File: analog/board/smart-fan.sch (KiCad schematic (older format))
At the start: 31 parts, among them J1 Conn_01x03_MountingPin, J2 Barrel_Jack, J3 Screw_Terminal_01x02, J4 Conn_01x03_Male, Q1 BC817, Q2 Q_PMOS_GSD, Q3 Q_PMOS_GSD, Q4 BC817, U1 MCP602, U2 AMS1117-5.0, U3 NE555P

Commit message: Working on analog board layout
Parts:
- J1: value Conn_01x03_MountingPin -> TEMP_In; footprint Connector_Pin127mm:PinHeader_1x03_P1.27mm_Vertical -> Connector_PinHeader_1.27mm:PinHeader_1x03_P1.27mm_Vertical; symbol ConnectorMountingPin:Conn_01x03_MountingPin -> smart-fan-rescue:Conn_01x03_MountingPin-ConnectorMountingPin
- J2: value Barrel_Jack -> 12V_PWR
- J3: value Screw_Terminal_01x02 -> 12V_In; footprint Connector_PinSocket254mm:PinSocket_1x02_P2.54mm_Vertical -> Connector_PinSocket_2.54mm:PinSocket_1x02_P2.54mm_Vertical
- J4: value Conn_01x03_Male -> FAN_Out; footprint Connector_Pin127mm:PinHeader_1x03_P1.27mm_Vertical -> Connector_JST:JST_EH_B3B-EH-A_1x03_P2.50mm_Vertical
- Q1, Q4: symbol TransistorBJT:BC817 -> smart-fan-rescue:BC817-TransistorBJT
- RV1: footprint Resistor_SMD:R_0805_2012Metric_Pad1.15x1.40mm_HandSolder -> Potentiometer_THT:Potentiometer_Bourns_3266Y_Vertical
- U1: footprint Package_SO:SOIC-8_3.9x4.9mm_P1.27mm -> Package_SO:SOIC-8_5.275x5.275mm_P1.27mm; symbol AmpOperational:MCP602 -> smart-fan-rescue:MCP602-AmpOperational
- U2: symbol Reg_Linear:AMS1117-5.0 -> smart-fan-rescue:AMS1117-5.0-Reg_Linear
- U3: footprint Package_DIP:DIP-8_W7.62mm -> Package_SO:SOIC-8_5.275x5.275mm_P1.27mm
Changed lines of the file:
@@
 $EndDescr
 $Comp
-L Reg_Linear:AMS1117-5.0 U2
+L smart-fan-rescue:AMS1117-5.0-Reg_Linear U2
 U 1 1 5EE1376A
 P 1400 1200
@@
 	850  1650 850  1500
 $Comp
-L AmpOperational:MCP602 U1
+L smart-fan-rescue:MCP602-AmpOperational U1
 U 1 1 5EE1D336
 P 3400 2450
 F 0 "U1" H 3400 2817 50  0000 C CNN
 F 1 "MCP602" H 3400 2726 50  0000 C CNN
-F 2 "Package_SO:SOIC-8_3.9x4.9mm_P1.27mm" H 3400 2450 50  0001 C CNN
+F 2 "Package_SO:SOIC-8_5.275x5.275mm_P1.27mm" H 3400 2450 50  0001 C CNN
 F 3 "http://ww1.microchip.com/downloads/en/DeviceDoc/21314g.pdf" H 3400 2450 50  0001 C CNN
 	1    3400 2450
@@
 $EndComp
 $Comp
-L AmpOperational:MCP602 U1
+L smart-fan-rescue:MCP602-AmpOperational U1
 U 2 1 5EE20815
 P 5150 2350
 F 0 "U1" H 5150 2717 50  0000 C CNN
 F 1 "MCP602" H 5150 2626 50  0000 C CNN
-F 2 "Package_SO:SOIC-8_3.9x4.9mm_P1.27mm" H 5150 2350 50  0001 C CNN
+F 2 "Package_SO:SOIC-8_5.275x5.275mm_P1.27mm" H 5150 2350 50  0001 C CNN
 F 3 "http://ww1.microchip.com/downloads/en/DeviceDoc/21314g.pdf" H 5150 2350 50  0001 C CNN
 	2    5150 2350
@@
 $EndComp
 $Comp
-L AmpOperational:MCP602 U1
+L smart-fan-rescue:MCP602-AmpOperational U1
 U 3 1 5EE2DBB3
 P 1000 3400
 F 0 "U1" H 958 3446 50  0000 L CNN
 F 1 "MCP602" H 958 3355 50  0000 L CNN
-F 2 "Package_SO:SOIC-8_3.9x4.9mm_P1.27mm" H 1000 3400 50  0001 C CNN
+F 2 "Package_SO:SOIC-8_5.275x5.275mm_P1.27mm" H 1000 3400 50  0001 C CNN
 F 3 "http://ww1.microchip.com/downloads/en/DeviceDoc/21314g.pdf" H 1000 3400 50  0001 C CNN
 	3    1000 3400
@@
 F 0 "RV1" H 4232 1896 50  0000 R CNN
 F 1 "10k" H 4232 1805 50  0000 R CNN
-F 2 "Resistor_SMD:R_0805_2012Metric_Pad1.15x1.40mm_HandSolder" H 4300 1850 50  0001 C CNN
+F 2 "Potentiometer_THT:Potentiometer_Bourns_3266Y_Vertical" H 4300 1850 50  0001 C CNN
 F 3 "~" H 4300 1850 50  0001 C CNN
 	1    4300 1850
@@
 $EndComp
 $Comp
-L TransistorBJT:BC817 Q4
+L smart-fan-rescue:BC817-TransistorBJT Q4
 U 1 1 5EE5A90C
 P 6900 2650
@@
 F 0 "U3" H 3000 5431 50  0000 C CNN
 F 1 "NE555P" H 3000 5340 50  0000 C CNN
-F 2 "Package_DIP:DIP-8_W7.62mm" H 3650 4450 50  0001 C CNN
+F 2 "Package_SO:SOIC-8_5.275x5.275mm_P1.27mm" H 3650 4450 50  0001 C CNN
 F 3 "http://www.ti.com/lit/ds/symlink/ne555.pdf" H 3850 4450 50  0001 C CNN
 	1    3000 4850
@@
 $EndComp
 $Comp
-L TransistorBJT:BC817 Q1
+L smart-fan-rescue:BC817-TransistorBJT Q1
 U 1 1 5EE8608C
 P 4950 4650
@@
 	3500 4650 4350 4650
 $Comp
-L ConnectorMountingPin:Conn_01x03_MountingPin J1
+L smart-fan-rescue:Conn_01x03_MountingPin-ConnectorMountingPin J1
 U 1 1 5EEE3110
 P 2150 2350
 F 0 "J1" H 2238 2222 50  0000 L CNN
-F 1 "Conn_01x03_MountingPin" H 2238 2313 50  0000 L CNN
-F 2 "Connector_Pin127mm:PinHeader_1x03_P1.27mm_Vertical" H 2150 2350 50  0001 C CNN
+F 1 "TEMP_In" H 2238 2313 50  0000 L CNN
+F 2 "Connector_PinHeader_1.27mm:PinHeader_1x03_P1.27mm_Vertical" H 2150 2350 50  0001 C CNN
 F 3 "~" H 2150 2350 50  0001 C CNN
 	1    2150 2350
@@
 P 3100 1000
 F 0 "J2" H 3157 1325 50  0000 C CNN
-F 1 "Barrel_Jack" H 3157 1234 50  0000 C CNN
+F 1 "12V_PWR" H 3157 1234 50  0000 C CNN
 F 2 "Connector_BarrelJack:BarrelJack_CUI_PJ-063AH_Horizontal_CircularHoles" H 3150 960 50  0001 C CNN
 F 3 "~" H 3150 960 50  0001 C CNN
@@
 P 4200 950
 F 0 "J3" H 4280 942 50  0000 L CNN
-F 1 "Screw_Terminal_01x02" H 4280 851 50  0000 L CNN
-F 2 "Connector_PinSocket254mm:PinSocket_1x02_P2.54mm_Vertical" H 4200 950 50  0001 C CNN
+F 1 "12V_In" H 4280 851 50  0000 L CNN
+F 2 "Connector_PinSocket_2.54mm:PinSocket_1x02_P2.54mm_Vertical" H 4200 950 50  0001 C CNN
 F 3 "~" H 4200 950 50  0001 C CNN
 	1    4200 950
@@
 Connection ~ 3550 1100
 $Comp
-L Power:+5V #PWR0101
+L smart-fan-rescue:+5V-Power #PWR0101
 U 1 1 5EF075B6
 P 4300 1450
@@
 $EndComp
 $Comp
-L Power:+5V #PWR0102
+L smart-fan-rescue:+5V-Power #PWR0102
 U 1 1 5EF08EF6
 P 6150 1650
@@
 $EndComp
 $Comp
-L Power:+5V #PWR0103
+L smart-fan-rescue:+5V-Power #PWR0103
 U 1 1 5EF093BB
 P 1900 850
@@
 $EndComp
 $Comp
-L Power:+5V #PWR0104
+L smart-fan-rescue:+5V-Power #PWR0104
 U 1 1 5EF099FD
 P 2500 2100
@@
 $EndComp
 $Comp
-L Power:+5V #PWR0105
+L smart-fan-rescue:+5V-Power #PWR0105
 U 1 1 5EF0D3EB
 P 1150 2750
@@
 	1150 2750 1150 2900
 $Comp
-L Power:GND #PWR0106
+L smart-fan-rescue:GND-Power #PWR0106
 U 1 1 5EF0F5D1
 P 5600 5550
@@
 $EndComp
 $Comp
-L Power:GND #PWR0107
+L smart-fan-rescue:GND-Power #PWR0107
 U 1 1 5EF10E2C
 P 3000 5850
@@
 $EndComp
 $Comp
-L Power:GND #PWR0108
+L smart-fan-rescue:GND-Power #PWR0108
 U 1 1 5EF1142C
 P 1150 3950
@@
 $EndComp
 $Comp
-L Power:GND #PWR0109
+L smart-fan-rescue:GND-Power #PWR0109
 U 1 1 5EF11B1A
 P 2950 3350
@@
 $EndComp
 $Comp
-L Power:GND #PWR0110
+L smart-fan-rescue:GND-Power #PWR0110
 U 1 1 5EF11F93
 P 6600 3400
@@
 $EndComp
 $Comp
-L Power:GND #PWR0111
+L smart-fan-rescue:GND-Power #PWR0111
 U 1 1 5EF123EA
 P 3550 1350
@@
 $EndComp
 $Comp
-L Power:GND #PWR0112
+L smart-fan-rescue:GND-Power #PWR0112
 U 1 1 5EF129EA
 P 1400 1850
@@
 $EndComp
 $Comp
-L Power:GND #PWR0113
+L smart-fan-rescue:GND-Power #PWR0113
 U 1 1 5EF12DA8
 P 4300 2100
@@
 $EndComp
 $Comp
-L Power:+12V #PWR0114
+L smart-fan-rescue:+12V-Power #PWR0114
 U 1 1 5EF14025
 P 850 850
@@
 $EndComp
 $Comp
-L Power:+12V #PWR0115
+L smart-fan-rescue:+12V-Power #PWR0115
 U 1 1 5EF1468B
 P 3550 700
@@
 $EndComp
 $Comp
-L Power:+12V #PWR0116
+L smart-fan-rescue:+12V-Power #PWR0116
 U 1 1 5EF14C4F
 P 5600 3700
@@
 $EndComp
 $Comp
-L Power:+12V #PWR0117
+L smart-fan-rescue:+12V-Power #PWR0117
 U 1 1 5EF151D4
 P 3000 3900
@@
 P 6300 4550
 F 0 "J4" H 6272 4482 50  0000 R CNN
-F 1 "Conn_01x03_Male" H 6272 4573 50  0000 R CNN
-F 2 "Connector_Pin127mm:PinHeader_1x03_P1.27mm_Vertical" H 6300 4550 50  0001 C CNN
+F 1 "FAN_Out" H 6272 4573 50  0000 R CNN
+F 2 "Connector_JST:JST_EH_B3B-EH-A_1x03_P2.50mm_Vertical" H 6300 4550 50  0001 C CNN
 F 3 "~" H 6300 4550 50  0001 C CNN
 	1    6300 4550

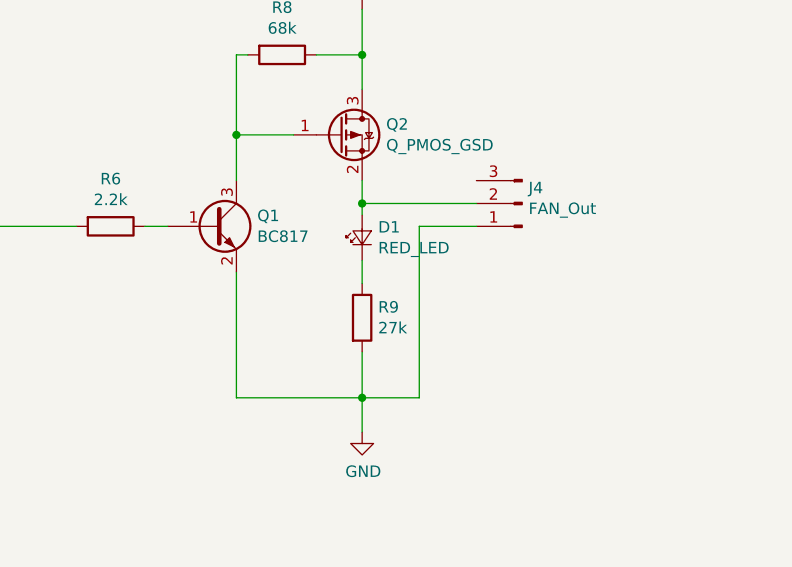
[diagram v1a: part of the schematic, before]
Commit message: Improving board layout
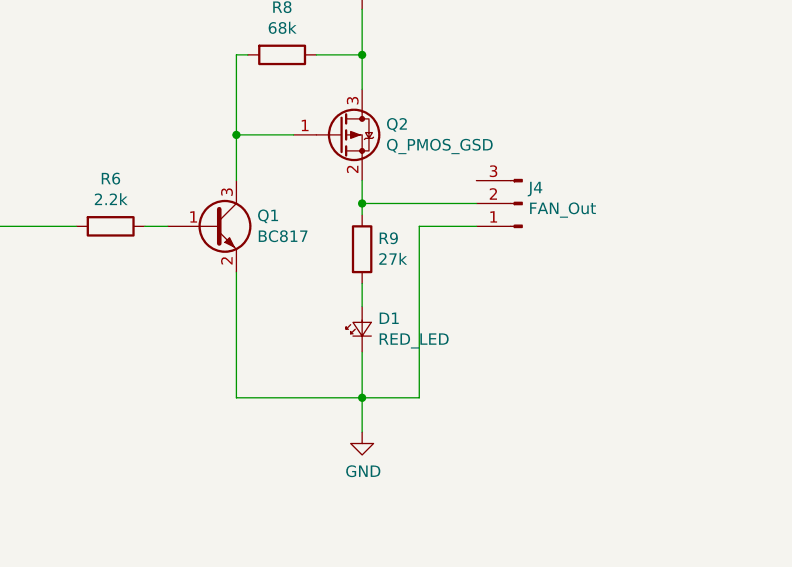
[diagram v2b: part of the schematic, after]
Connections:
- net GND: now also D1.1 (K); no longer R9.2
- net at J4.2 (Pin_2), Q2.2 (S): now also R9.1; no longer D1.2 (A)
- new net: D1.2 (A), R9.2
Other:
- moved on the sheet: D1, R9
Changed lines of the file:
@@
 L Device:R R9
 U 1 1 5EE89D31
-P 5600 5050
-F 0 "R9" H 5670 5096 50  0000 L CNN
-F 1 "27k" H 5670 5005 50  0000 L CNN
-F 2 "Resistor_SMD:R_0805_2012Metric_Pad1.15x1.40mm_HandSolder" V 5530 5050 50  0001 C CNN
-F 3 "~" H 5600 5050 50  0001 C CNN
-	1    5600 5050
+P 5600 4750
+F 0 "R9" H 5670 4796 50  0000 L CNN
+F 1 "27k" H 5670 4705 50  0000 L CNN
+F 2 "Resistor_SMD:R_0805_2012Metric_Pad1.15x1.40mm_HandSolder" V 5530 4750 50  0001 C CNN
+F 3 "~" H 5600 4750 50  0001 C CNN
+	1    5600 4750
 	1    0    0    -1
 $EndComp
@@
 L Device:LED_Small D1
 U 1 1 5EE8AC2E
-P 5600 4700
-F 0 "D1" V 5646 4630 50  0000 R CNN
-F 1 "RED_LED" V 5555 4630 50  0000 R CNN
-F 2 "Resistor_SMD:R_0805_2012Metric_Pad1.15x1.40mm_HandSolder" V 5600 4700 50  0001 C CNN
-F 3 "~" V 5600 4700 50  0001 C CNN
-	1    5600 4700
+P 5600 5100
+F 0 "D1" V 5646 5030 50  0000 R CNN
+F 1 "RED_LED" V 5555 5030 50  0000 R CNN
+F 2 "Resistor_SMD:R_0805_2012Metric_Pad1.15x1.40mm_HandSolder" V 5600 5100 50  0001 C CNN
+F 3 "~" V 5600 5100 50  0001 C CNN
+	1    5600 5100
 	0    -1   -1   0
 $EndComp
@@
 Wire Wire Line
 	5600 5400 5600 5200
-Wire Wire Line
-	5600 4900 5600 4800
 Wire Wire Line
 	5600 4600 5600 4550
@@
 	1    0    0    -1
 $EndComp
+Wire Wire Line
+	5600 4900 5600 5000
 $EndSCHEMATC

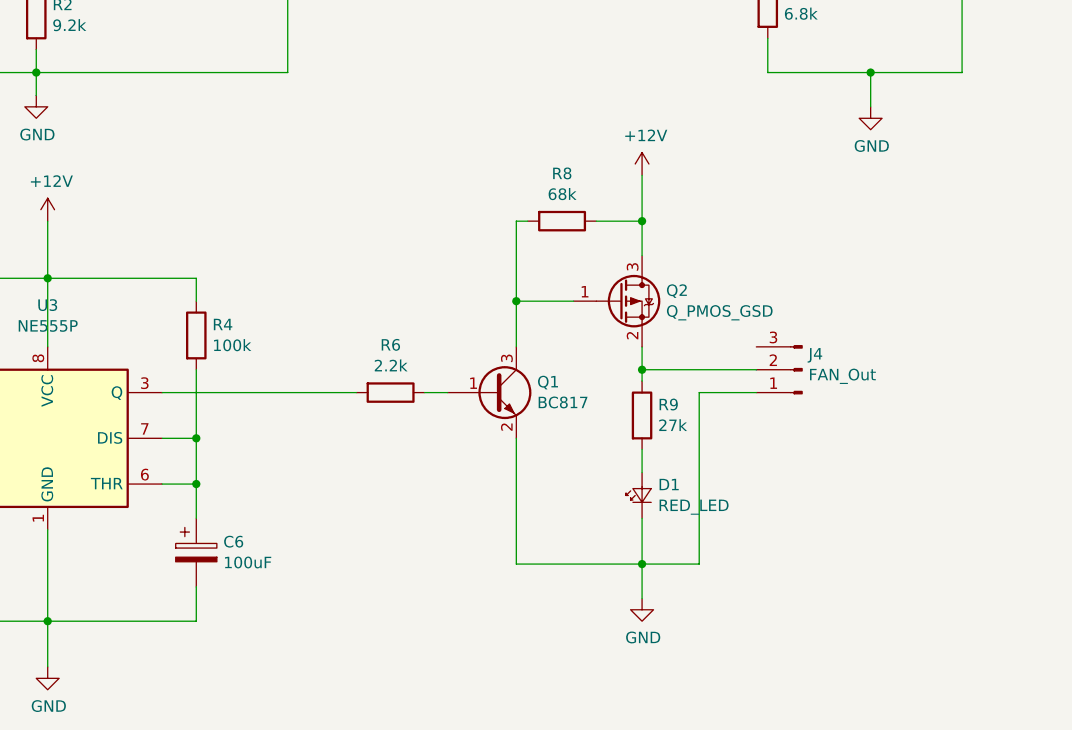
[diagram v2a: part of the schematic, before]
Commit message: Board layout complete with ground planes and mounting holes
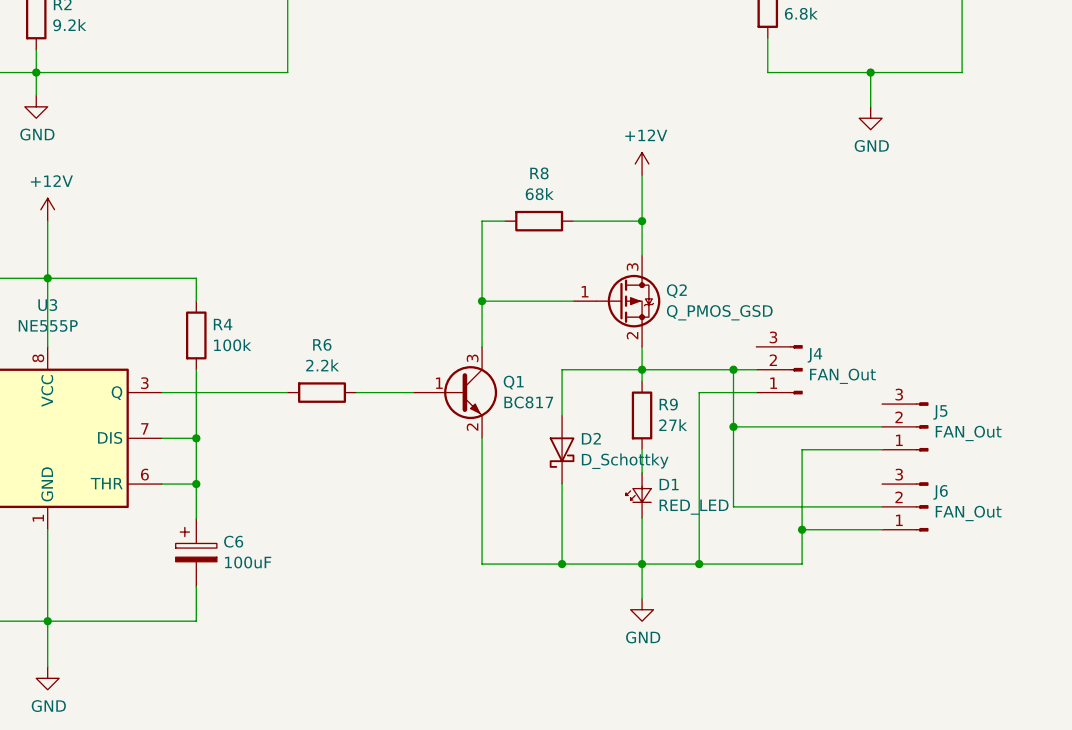
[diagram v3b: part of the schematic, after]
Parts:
- added D2: D_Schottky, Diode_SMD:D_1210_3225Metric_Pad1.42x2.65mm_HandSolder, symbol Device:D_Schottky
- added J5, J6: FAN_Out, Connector:FanPinHeader_1x03_P2.54mm_Vertical, symbol Connector:Conn_01x03_Male
- J4: footprint Connector_JST:JST_EH_B3B-EH-A_1x03_P2.50mm_Vertical -> Connector:FanPinHeader_1x03_P2.54mm_Vertical
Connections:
- net GND: now also D2.1 (K), J5.1 (Pin_1), J6.1 (Pin_1)
- net at J4.2 (Pin_2), Q2.2 (S), R9.1: now also D2.2 (A), J5.2 (Pin_2), J6.2 (Pin_2)
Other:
- moved on the sheet: Q1, R6, R8
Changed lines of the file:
@@
 L smart-fan-rescue:BC817-TransistorBJT Q1
 U 1 1 5EE8608C
-P 4950 4650
-F 0 "Q1" H 5141 4696 50  0000 L CNN
-F 1 "BC817" H 5141 4605 50  0000 L CNN
-F 2 "Package_TO_SOT_SMD:SOT-23" H 5150 4575 50  0001 L CIN
-F 3 "http://www.fairchildsemi.com/ds/BC/BC817.pdf" H 4950 4650 50  0001 L CNN
-	1    4950 4650
+P 4800 4650
+F 0 "Q1" H 4991 4696 50  0000 L CNN
+F 1 "BC817" H 4991 4605 50  0000 L CNN
+F 2 "Package_TO_SOT_SMD:SOT-23" H 5000 4575 50  0001 L CIN
+F 3 "http://www.fairchildsemi.com/ds/BC/BC817.pdf" H 4800 4650 50  0001 L CNN
+	1    4800 4650
 	1    0    0    -1
 $EndComp
@@
 L Device:R R8
 U 1 1 5EE883E5
-P 5250 3900
-F 0 "R8" V 5043 3900 50  0000 C CNN
-F 1 "68k" V 5134 3900 50  0000 C CNN
-F 2 "Resistor_SMD:R_0805_2012Metric_Pad1.15x1.40mm_HandSolder" V 5180 3900 50  0001 C CNN
-F 3 "~" H 5250 3900 50  0001 C CNN
-	1    5250 3900
-	0    1    1    0
-$EndComp
-$Comp
-L Device:R R6
-U 1 1 5EE88F47
-P 4500 4650
-F 0 "R6" V 4293 4650 50  0000 C CNN
-F 1 "2.2k" V 4384 4650 50  0000 C CNN
-F 2 "Resistor_SMD:R_0805_2012Metric_Pad1.15x1.40mm_HandSolder" V 4430 4650 50  0001 C CNN
-F 3 "~" H 4500 4650 50  0001 C CNN
-	1    4500 4650
+P 5150 3900
+F 0 "R8" V 4943 3900 50  0000 C CNN
+F 1 "68k" V 5034 3900 50  0000 C CNN
+F 2 "Resistor_SMD:R_0805_2012Metric_Pad1.15x1.40mm_HandSolder" V 5080 3900 50  0001 C CNN
+F 3 "~" H 5150 3900 50  0001 C CNN
+	1    5150 3900
 	0    1    1    0
 $EndComp
@@
 	5600 4050 5600 3900
 Wire Wire Line
-	5600 3900 5400 3900
-Wire Wire Line
-	5300 4250 5050 4250
-Wire Wire Line
-	5050 4250 5050 4450
-Wire Wire Line
-	5050 4250 5050 3900
-Wire Wire Line
-	5050 3900 5100 3900
-Connection ~ 5050 4250
-Wire Wire Line
-	4750 4650 4650 4650
-Wire Wire Line
-	5050 4850 5050 5400
-Wire Wire Line
-	5050 5400 5600 5400
+	5600 3900 5300 3900
+Wire Wire Line
+	5300 4250 4900 4250
+Wire Wire Line
+	4900 4250 4900 4450
+Wire Wire Line
+	4900 4250 4900 3900
+Wire Wire Line
+	4900 3900 5000 3900
+Connection ~ 4900 4250
+Wire Wire Line
+	4600 4650 4350 4650
+Wire Wire Line
+	4900 4850 4900 5400
+Wire Wire Line
+	4900 5400 5250 5400
 Wire Wire Line
 	5600 5400 5600 5200
@@
 	5600 4600 5600 4550
 Wire Wire Line
-	5600 4550 6100 4550
+	5600 4550 6000 4550
 Connection ~ 5600 4550
 Wire Wire Line
@@
 	2350 4650 1800 4650
 Connection ~ 2350 4650
-Wire Wire Line
-	3500 4650 4350 4650
 $Comp
 L smart-fan-rescue:Conn_01x03_MountingPin-ConnectorMountingPin J1
@@
 F 0 "J4" H 6272 4482 50  0000 R CNN
 F 1 "FAN_Out" H 6272 4573 50  0000 R CNN
-F 2 "Connector_JST:JST_EH_B3B-EH-A_1x03_P2.50mm_Vertical" H 6300 4550 50  0001 C CNN
+F 2 "Connector:FanPinHeader_1x03_P2.54mm_Vertical" H 6300 4550 50  0001 C CNN
 F 3 "~" H 6300 4550 50  0001 C CNN
 	1    6300 4550
@@
 Wire Wire Line
 	5600 4900 5600 5000
+$Comp
+L Connector:Conn_01x03_Male J5
+U 1 1 5EEA3848
+P 6850 4800
+F 0 "J5" H 6822 4732 50  0000 R CNN
+F 1 "FAN_Out" H 6822 4823 50  0000 R CNN
+F 2 "Connector:FanPinHeader_1x03_P2.54mm_Vertical" H 6850 4800 50  0001 C CNN
+F 3 "~" H 6850 4800 50  0001 C CNN
+	1    6850 4800
+	-1   0    0    1
+$EndComp
+$Comp
+L Connector:Conn_01x03_Male J6
+U 1 1 5EEA4260
+P 6850 5150
+F 0 "J6" H 6822 5082 50  0000 R CNN
+F 1 "FAN_Out" H 6822 5173 50  0000 R CNN
+F 2 "Connector:FanPinHeader_1x03_P2.54mm_Vertical" H 6850 5150 50  0001 C CNN
+F 3 "~" H 6850 5150 50  0001 C CNN
+	1    6850 5150
+	-1   0    0    1
+$EndComp
+Wire Wire Line
+	5850 5400 6300 5400
+Connection ~ 5850 5400
+Wire Wire Line
+	6650 5250 6300 5250
+Wire Wire Line
+	6300 5250 6300 5400
+Wire Wire Line
+	6650 4900 6300 4900
+Wire Wire Line
+	6300 4900 6300 5250
+Connection ~ 6300 5250
+Wire Wire Line
+	6650 5150 6000 5150
+Wire Wire Line
+	6000 5150 6000 4800
+Connection ~ 6000 4550
+Wire Wire Line
+	6000 4550 6100 4550
+Wire Wire Line
+	6650 4800 6000 4800
+Connection ~ 6000 4800
+Wire Wire Line
+	6000 4800 6000 4550
+$Comp
+L Device:D_Schottky D2
+U 1 1 5EEDDC4D
+P 5250 4900
+F 0 "D2" V 5296 4820 50  0000 R CNN
+F 1 "D_Schottky" V 5205 4820 50  0000 R CNN
+F 2 "Diode_SMD:D_1210_3225Metric_Pad1.42x2.65mm_HandSolder" H 5250 4900 50  0001 C CNN
+F 3 "~" H 5250 4900 50  0001 C CNN
+	1    5250 4900
+	0    -1   -1   0
+$EndComp
+Wire Wire Line
+	3500 4650 4050 4650
+$Comp
+L Device:R R6
+U 1 1 5EE88F47
+P 4200 4650
+F 0 "R6" V 3993 4650 50  0000 C CNN
+F 1 "2.2k" V 4084 4650 50  0000 C CNN
+F 2 "Resistor_SMD:R_0805_2012Metric_Pad1.15x1.40mm_HandSolder" V 4130 4650 50  0001 C CNN
+F 3 "~" H 4200 4650 50  0001 C CNN
+	1    4200 4650
+	0    1    1    0
+$EndComp
+Wire Wire Line
+	5600 4550 5250 4550
+Wire Wire Line
+	5250 4550 5250 4750
+Wire Wire Line
+	5250 5050 5250 5400
+Connection ~ 5250 5400
+Wire Wire Line
+	5250 5400 5600 5400
 $EndSCHEMATC

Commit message: WIP: Cleaning up board
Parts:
- removed U3: NE555P, Package_SO:SOIC-8_5.275x5.275mm_P1.27mm, symbol Timer:NE555P
- added U?: LM555, symbol Timer:LM555
- R2: value 9.2k -> 10k
- R3: value 82k -> 10k
- R5: value 2.2k -> 1k
- R7: value 2.2k -> 100k
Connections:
- net +12V: now also U?.4 (R), U?.8 (VCC)
- net GND: now also D2.2 (A), U?.1 (GND); no longer D2.1 (K)
- net Trigger: now also U?.2 (TR)
- net at J4.2 (Pin_2), J5.2 (Pin_2), J6.2 (Pin_2)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: now also D2.1 (K); no longer D2.2 (A)
- net at R6.2: now also U?.3 (Q)
- net at C4.1: now also U?.5 (CV)
- net at C6.1, R4.2: now also U?.6 (THR), U?.7 (DIS)
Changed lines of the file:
@@
 EELAYER 30 0
 EELAYER END
-$Descr A0 46811 33110
+$Descr A3 16535 11693
 encoding utf-8
 Sheet 1 1
@@
 P 4350 2450
 F 0 "R5" V 4557 2450 50  0000 C CNN
-F 1 "2.2k" V 4466 2450 50  0000 C CNN
+F 1 "1k" V 4466 2450 50  0000 C CNN
 F 2 "Resistor_SMD:R_0805_2012Metric_Pad1.15x1.40mm_HandSolder" V 4280 2450 50  0001 C CNN
 F 3 "~" H 4350 2450 50  0001 C CNN
@@
 P 2950 3000
 F 0 "R2" H 3020 3046 50  0000 L CNN
-F 1 "9.2k" H 3020 2955 50  0000 L CNN
+F 1 "10k" H 3020 2955 50  0000 L CNN
 F 2 "Resistor_SMD:R_0805_2012Metric_Pad1.15x1.40mm_HandSolder" V 2880 3000 50  0001 C CNN
 F 3 "~" H 2950 3000 50  0001 C CNN
@@
 P 3400 2750
 F 0 "R3" V 3193 2750 50  0000 C CNN
-F 1 "82k" V 3284 2750 50  0000 C CNN
+F 1 "10k" V 3284 2750 50  0000 C CNN
 F 2 "Resistor_SMD:R_0805_2012Metric_Pad1.15x1.40mm_HandSolder" V 3330 2750 50  0001 C CNN
 F 3 "~" H 3400 2750 50  0001 C CNN
@@
 P 5150 2750
 F 0 "R7" V 4943 2750 50  0000 C CNN
-F 1 "2.2k" V 5034 2750 50  0000 C CNN
+F 1 "100k" V 5034 2750 50  0000 C CNN
 F 2 "Resistor_SMD:R_0805_2012Metric_Pad1.15x1.40mm_HandSolder" V 5080 2750 50  0001 C CNN
 F 3 "~" H 5150 2750 50  0001 C CNN
@@
 	1150 3800 900  3800
 $Comp
-L Timer:NE555P U3
-U 1 1 5EE81F54
-P 3000 4850
-F 0 "U3" H 3000 5431 50  0000 C CNN
-F 1 "NE555P" H 3000 5340 50  0000 C CNN
-F 2 "Package_SO:SOIC-8_5.275x5.275mm_P1.27mm" H 3650 4450 50  0001 C CNN
-F 3 "http://www.ti.com/lit/ds/symlink/ne555.pdf" H 3850 4450 50  0001 C CNN
-	1    3000 4850
-	1    0    0    -1
-$EndComp
-$Comp
 L smart-fan-rescue:BC817-TransistorBJT Q1
 U 1 1 5EE8608C
@@
 F 3 "~" H 5250 4900 50  0001 C CNN
 	1    5250 4900
-	0    -1   -1   0
+	0    1    1    0
 $EndComp
 Wire Wire Line
@@
 Wire Wire Line
 	5250 5400 5600 5400
+$Comp
+L Timer:LM555 U?
+U 1 1 5F277BFB
+P 3000 4850
+F 0 "U?" H 3000 5431 50  0000 C CNN
+F 1 "LM555" H 3000 5340 50  0000 C CNN
+F 2 "" H 3000 4850 50  0001 C CNN
+F 3 "http://www.ti.com/lit/ds/symlink/lm555.pdf" H 3000 4850 50  0001 C CNN
+	1    3000 4850
+	1    0    0    -1
+$EndComp
 $EndSCHEMATC
